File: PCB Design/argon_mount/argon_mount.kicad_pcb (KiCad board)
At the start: 2 copper layers, 34.6 x 71.1 mm, 5 parts, among them CN2 1X4SMT, U1 MIC5219-2.85YM5, U2 VL6180

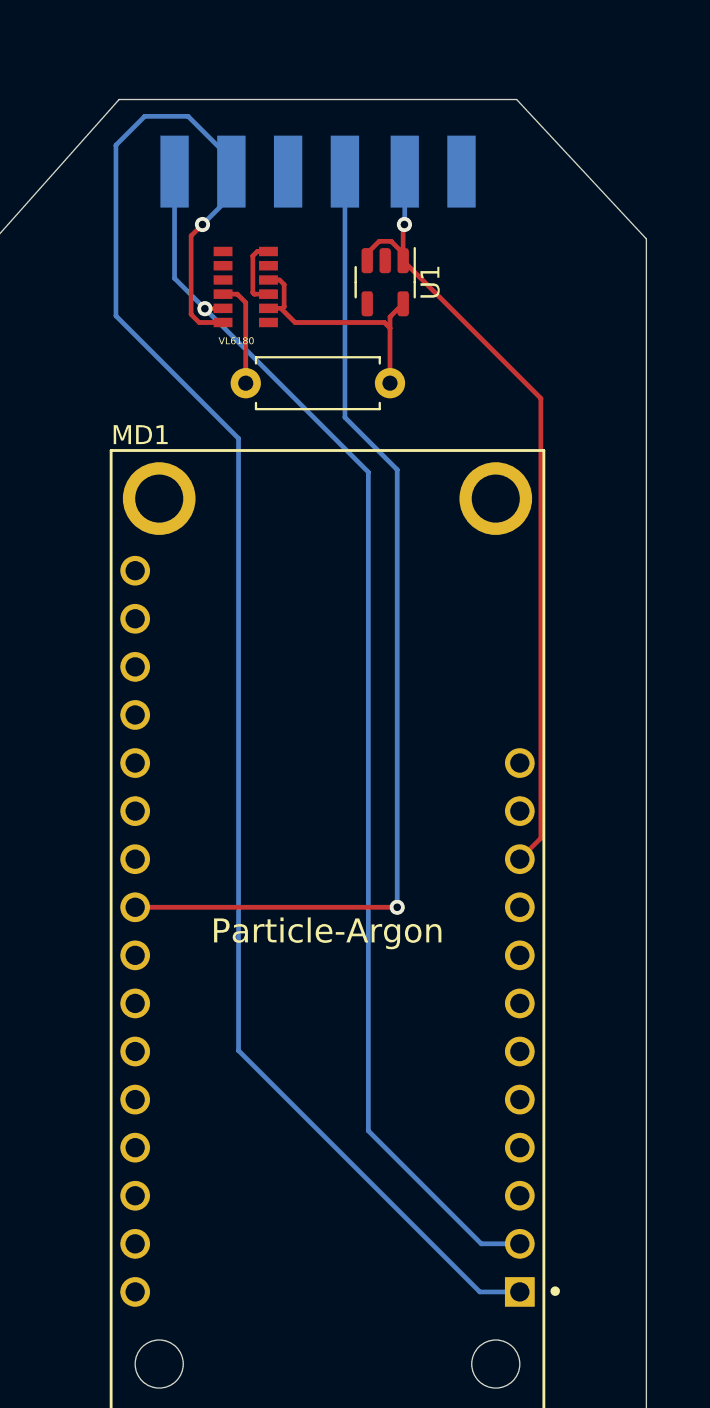
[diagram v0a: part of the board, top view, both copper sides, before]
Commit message: argon pcb fix
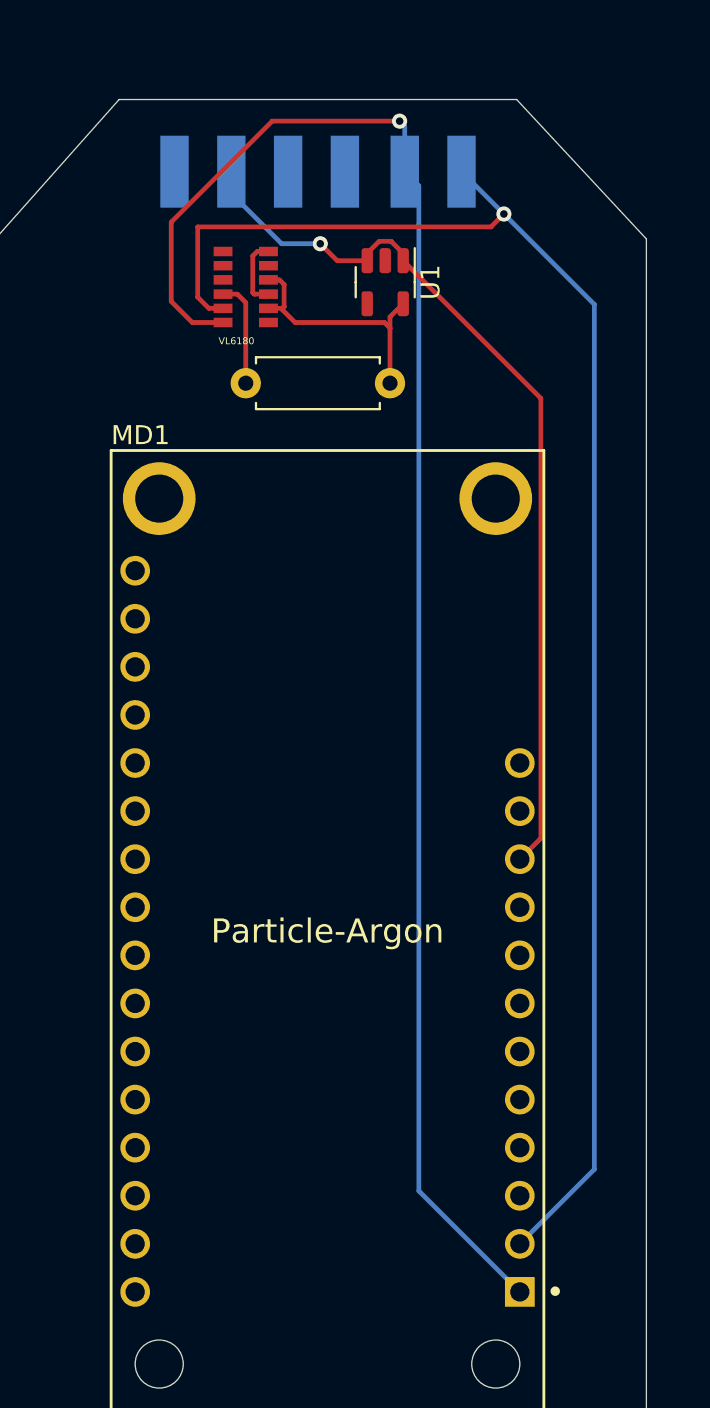
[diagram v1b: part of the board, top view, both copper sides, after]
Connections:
- CN2 pad 1: GND -> /SCL
- CN2 pad 2: +5V -> /SDA
- CN2 pad 3: Net-(CN2-Pad3) -> GND
- CN2 pad 4: GND -> unconnected-(CN2-Pad4)
- CN2 pad 5: /SDA -> +5V
- CN2 pad 6: /SCL -> GND
- MD1 pad 16: Net-(CN2-Pad3) -> unconnected-(MD1-Pad16)
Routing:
- net Net-(CN2-Pad3): track 53.8 -> 0.00 mm, vias 1 -> 0
- net /SCL: track 66.3 -> 82.9 mm
- net +5V: track 42.3 -> 47.3 mm
- net /SDA: track 88.6 -> 86.1 mm

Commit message: mount fix + offshoot flip
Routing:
- net /SCL: track 82.9 -> 84.6 mm
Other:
- outline, holes or cut-outs redrawn
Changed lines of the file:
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@@
       (net 2 "GND") (pinfunction "6") (pintype "bidirectional") (solder_mask_margin 0.1016))
   )
+  (gr_line (start 129.2 89.915998) (end 129.2 97.535998) (layer "Edge.Cuts") (width 0.05))
+  (gr_line (start 129.2 97.535998) (end 122.428 97.536) (layer "Edge.Cuts") (width 0.05))
   (gr_line (start 129.2 89.915998) (end 150.2 89.915999) (layer "Edge.Cuts") (width 0.05))
   (gr_line (start 122.428 97.536) (end 122.428 161.036) (layer "Edge.Cuts") (width 0.05))
-  (gr_line (start 150.2 89.915999) (end 157.054 97.282) (layer "Edge.Cuts") (width 0.05))
   (gr_line (start 122.428 161.036) (end 157.054 161.036) (layer "Edge.Cuts") (width 0.05))
-  (gr_line (start 157.054 97.282) (end 157.054 161.036) (layer "Edge.Cuts") (width 0.05))
-  (gr_line (start 122.428 97.536) (end 129.2 89.915998) (layer "Edge.Cuts") (width 0.05))
+  (gr_line (start 157.054 97.536) (end 157.054 161.036) (layer "Edge.Cuts") (width 0.05))
+  (gr_line (start 150.2 97.535999) (end 157.054 97.536) (layer "Edge.Cuts") (width 0.05))
+  (gr_line (start 150.2 89.915999) (end 150.2 97.535999) (layer "Edge.Cuts") (width 0.05))
   (segment (start 143.573277 97.409) (end 142.938723 97.409) (width 0.25) (layer "F.Cu") (net 1))
   (segment (start 140.7215 98.4305) (end 139.827 97.536) (width 0.25) (layer "F.Cu") (net 1))
@@
   (segment (start 149.5265 95.9645) (end 148.844 96.647) (width 0.25) (layer "F.Cu") (net 4))
   (via (at 149.5265 95.9645) (size 0.8) (drill 0.4) (layers "F.Cu" "B.Cu") (net 4))
-  (segment (start 154.305 100.743) (end 149.5265 95.9645) (width 0.25) (layer "B.Cu") (net 4))
+  (segment (start 149.5265 98.8535) (end 149.5265 95.9645) (width 0.25) (layer "B.Cu") (net 4))
   (segment (start 149.5265 95.9645) (end 147.288 93.726) (width 0.25) (layer "B.Cu") (net 4))
+  (segment (start 151.416 100.743) (end 149.5265 98.8535) (width 0.25) (layer "B.Cu") (net 4))
   (segment (start 154.305 146.431) (end 154.305 100.743) (width 0.25) (layer "B.Cu") (net 4))
   (segment (start 150.368 150.368) (end 154.305 146.431) (width 0.25) (layer "B.Cu") (net 4))
+  (segment (start 154.305 100.743) (end 151.416 100.743) (width 0.25) (layer "B.Cu") (net 4))
   (segment (start 137.9182 99.6912) (end 137.674 99.447) (width 0.25) (layer "F.Cu") (net 31))
   (segment (start 143.51 101.9909) (end 143.51 101.4015) (width 0.25) (layer "F.Cu") (net 31))
